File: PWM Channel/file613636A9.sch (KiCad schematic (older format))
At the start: 4 parts

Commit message: Starting rough routing
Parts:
- gave numbers to parts that had none: 4
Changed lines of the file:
@@
 U 1 1 61365705
 P 4050 3650
-F 0 "#PWR?" H 4050 3400 50  0001 C CNN
+AR Path="/61351170/61365705" Ref="#PWR?"  Part="1"
+AR Path="/613636AA/61365705" Ref="#PWR0103"  Part="1"
+F 0 "#PWR0103" H 4050 3400 50  0001 C CNN
 F 1 "GND" V 4055 3522 50  0000 R CNN
 F 2 "" H 4050 3650 50  0001 C CNN
@@
 U 1 1 6136570C
 P 3550 2750
-F 0 "#PWR?" H 3550 2600 50  0001 C CNN
+AR Path="/61351170/6136570C" Ref="#PWR?"  Part="1"
+AR Path="/613636AA/6136570C" Ref="#PWR0104"  Part="1"
+F 0 "#PWR0104" H 3550 2600 50  0001 C CNN
 F 1 "+5V" V 3565 2878 50  0000 L CNN
 F 2 "" H 3550 2750 50  0001 C CNN
@@
 AR Path="/613546BD/61365713" Ref="C?"  Part="1"
 AR Path="/61351170/61365713" Ref="C?"  Part="1"
-F 0 "C?" H 3635 1904 50  0000 R CNN
+AR Path="/613636AA/61365713" Ref="C401"  Part="1"
+F 0 "C401" H 3635 1904 50  0000 R CNN
 F 1 "0.1uF" H 3635 1995 50  0000 R CNN
 F 2 "Capacitor_THT:C_Disc_D4.3mm_W1.9mm_P5.00mm" H 3788 1800 50  0001 C CNN
@@
 U 1 1 61365719
 P 4050 1700
-F 0 "#PWR?" H 4050 1550 50  0001 C CNN
+AR Path="/61351170/61365719" Ref="#PWR?"  Part="1"
+AR Path="/613636AA/61365719" Ref="#PWR0105"  Part="1"
+F 0 "#PWR0105" H 4050 1550 50  0001 C CNN
 F 1 "+5V" H 4065 1873 50  0000 C CNN
 F 2 "" H 4050 1700 50  0001 C CNN
@@
 U 1 1 61365724
 P 3200 3050
-F 0 "#PWR?" H 3200 2800 50  0001 C CNN
+AR Path="/61351170/61365724" Ref="#PWR?"  Part="1"
+AR Path="/613636AA/61365724" Ref="#PWR0106"  Part="1"
+F 0 "#PWR0106" H 3200 2800 50  0001 C CNN
 F 1 "GND" V 3205 2922 50  0000 R CNN
 F 2 "" H 3200 3050 50  0001 C CNN
@@
 U 1 1 6136572B
 P 4050 2850
-F 0 "U?" H 4050 3631 50  0000 C CNN
+AR Path="/61351170/6136572B" Ref="U?"  Part="1"
+AR Path="/613636AA/6136572B" Ref="U401"  Part="1"
+F 0 "U401" H 4050 3631 50  0000 C CNN
 F 1 "74HCT595" H 4050 3540 50  0000 C CNN
 F 2 "Package_DIP:DIP-16_W7.62mm_Socket" H 4050 2850 50  0001 C CNN
@@
 U 1 1 61365731
 P 3500 2100
-F 0 "#PWR?" H 3500 1850 50  0001 C CNN
+AR Path="/61351170/61365731" Ref="#PWR?"  Part="1"
+AR Path="/613636AA/61365731" Ref="#PWR0107"  Part="1"
+F 0 "#PWR0107" H 3500 1850 50  0001 C CNN
 F 1 "GND" V 3505 1972 50  0000 R CNN
 F 2 "" H 3500 2100 50  0001 C CNN
@@
 U 1 1 6136573C
 P 4050 6150
-F 0 "#PWR?" H 4050 5900 50  0001 C CNN
+AR Path="/61351170/6136573C" Ref="#PWR?"  Part="1"
+AR Path="/613636AA/6136573C" Ref="#PWR0108"  Part="1"
+F 0 "#PWR0108" H 4050 5900 50  0001 C CNN
 F 1 "GND" V 4055 6022 50  0000 R CNN
 F 2 "" H 4050 6150 50  0001 C CNN
@@
 U 1 1 61365743
 P 3550 5250
-F 0 "#PWR?" H 3550 5100 50  0001 C CNN
+AR Path="/61351170/61365743" Ref="#PWR?"  Part="1"
+AR Path="/613636AA/61365743" Ref="#PWR0109"  Part="1"
+F 0 "#PWR0109" H 3550 5100 50  0001 C CNN
 F 1 "+5V" V 3565 5378 50  0000 L CNN
 F 2 "" H 3550 5250 50  0001 C CNN
@@
 AR Path="/613546BD/6136574A" Ref="C?"  Part="1"
 AR Path="/61351170/6136574A" Ref="C?"  Part="1"
-F 0 "C?" H 3635 4404 50  0000 R CNN
+AR Path="/613636AA/6136574A" Ref="C402"  Part="1"
+F 0 "C402" H 3635 4404 50  0000 R CNN
 F 1 "0.1uF" H 3635 4495 50  0000 R CNN
 F 2 "Capacitor_THT:C_Disc_D4.3mm_W1.9mm_P5.00mm" H 3788 4300 50  0001 C CNN
@@
 U 1 1 61365750
 P 4050 4200
-F 0 "#PWR?" H 4050 4050 50  0001 C CNN
+AR Path="/61351170/61365750" Ref="#PWR?"  Part="1"
+AR Path="/613636AA/61365750" Ref="#PWR0110"  Part="1"
+F 0 "#PWR0110" H 4050 4050 50  0001 C CNN
 F 1 "+5V" H 4065 4373 50  0000 C CNN
 F 2 "" H 4050 4200 50  0001 C CNN
@@
 U 1 1 6136575B
 P 3200 5550
-F 0 "#PWR?" H 3200 5300 50  0001 C CNN
+AR Path="/61351170/6136575B" Ref="#PWR?"  Part="1"
+AR Path="/613636AA/6136575B" Ref="#PWR0111"  Part="1"
+F 0 "#PWR0111" H 3200 5300 50  0001 C CNN
 F 1 "GND" V 3205 5422 50  0000 R CNN
 F 2 "" H 3200 5550 50  0001 C CNN
@@
 U 1 1 61365762
 P 4050 5350
-F 0 "U?" H 4050 6131 50  0000 C CNN
+AR Path="/61351170/61365762" Ref="U?"  Part="1"
+AR Path="/613636AA/61365762" Ref="U402"  Part="1"
+F 0 "U402" H 4050 6131 50  0000 C CNN
 F 1 "74HCT595" H 4050 6040 50  0000 C CNN
 F 2 "Package_DIP:DIP-16_W7.62mm_Socket" H 4050 5350 50  0001 C CNN
@@
 U 1 1 61365769
 P 3500 4600
-F 0 "#PWR?" H 3500 4350 50  0001 C CNN
+AR Path="/61351170/61365769" Ref="#PWR?"  Part="1"
+AR Path="/613636AA/61365769" Ref="#PWR0112"  Part="1"
+F 0 "#PWR0112" H 3500 4350 50  0001 C CNN
 F 1 "GND" V 3505 4472 50  0000 R CNN
 F 2 "" H 3500 4600 50  0001 C CNN

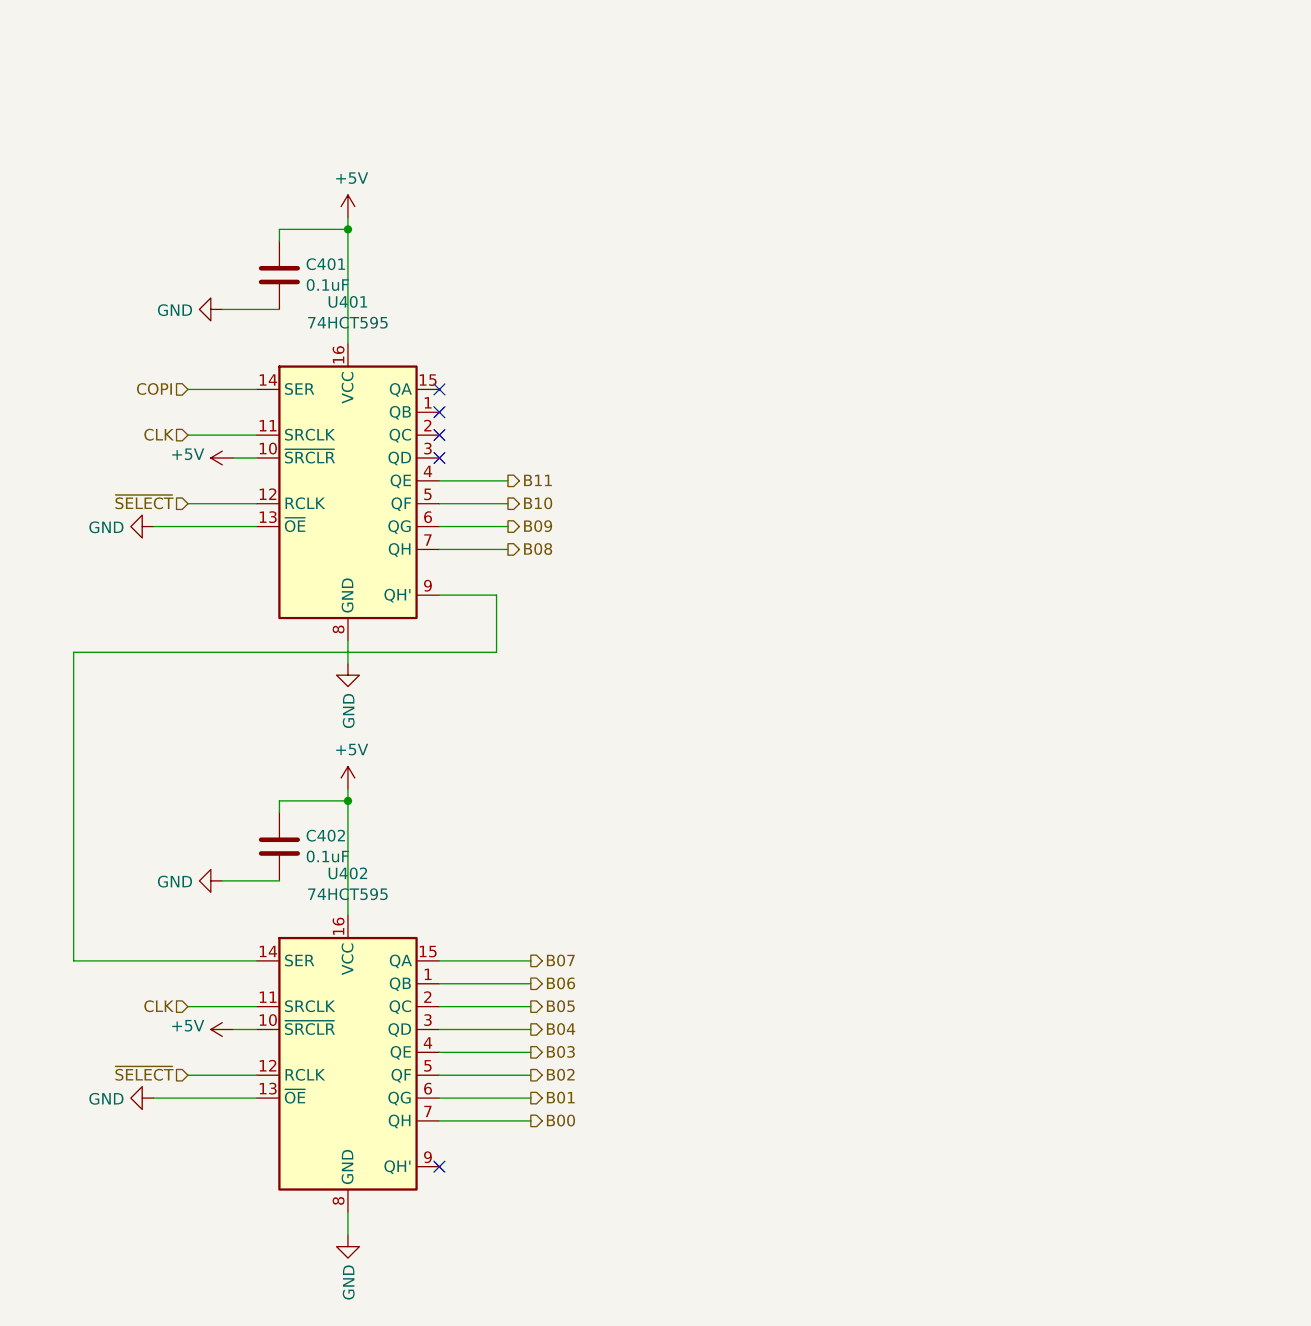
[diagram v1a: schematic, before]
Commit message: Updates to PWM Channel Board (#6)
Add a number of LED indicators and reduce from 12-bit to 8-bit
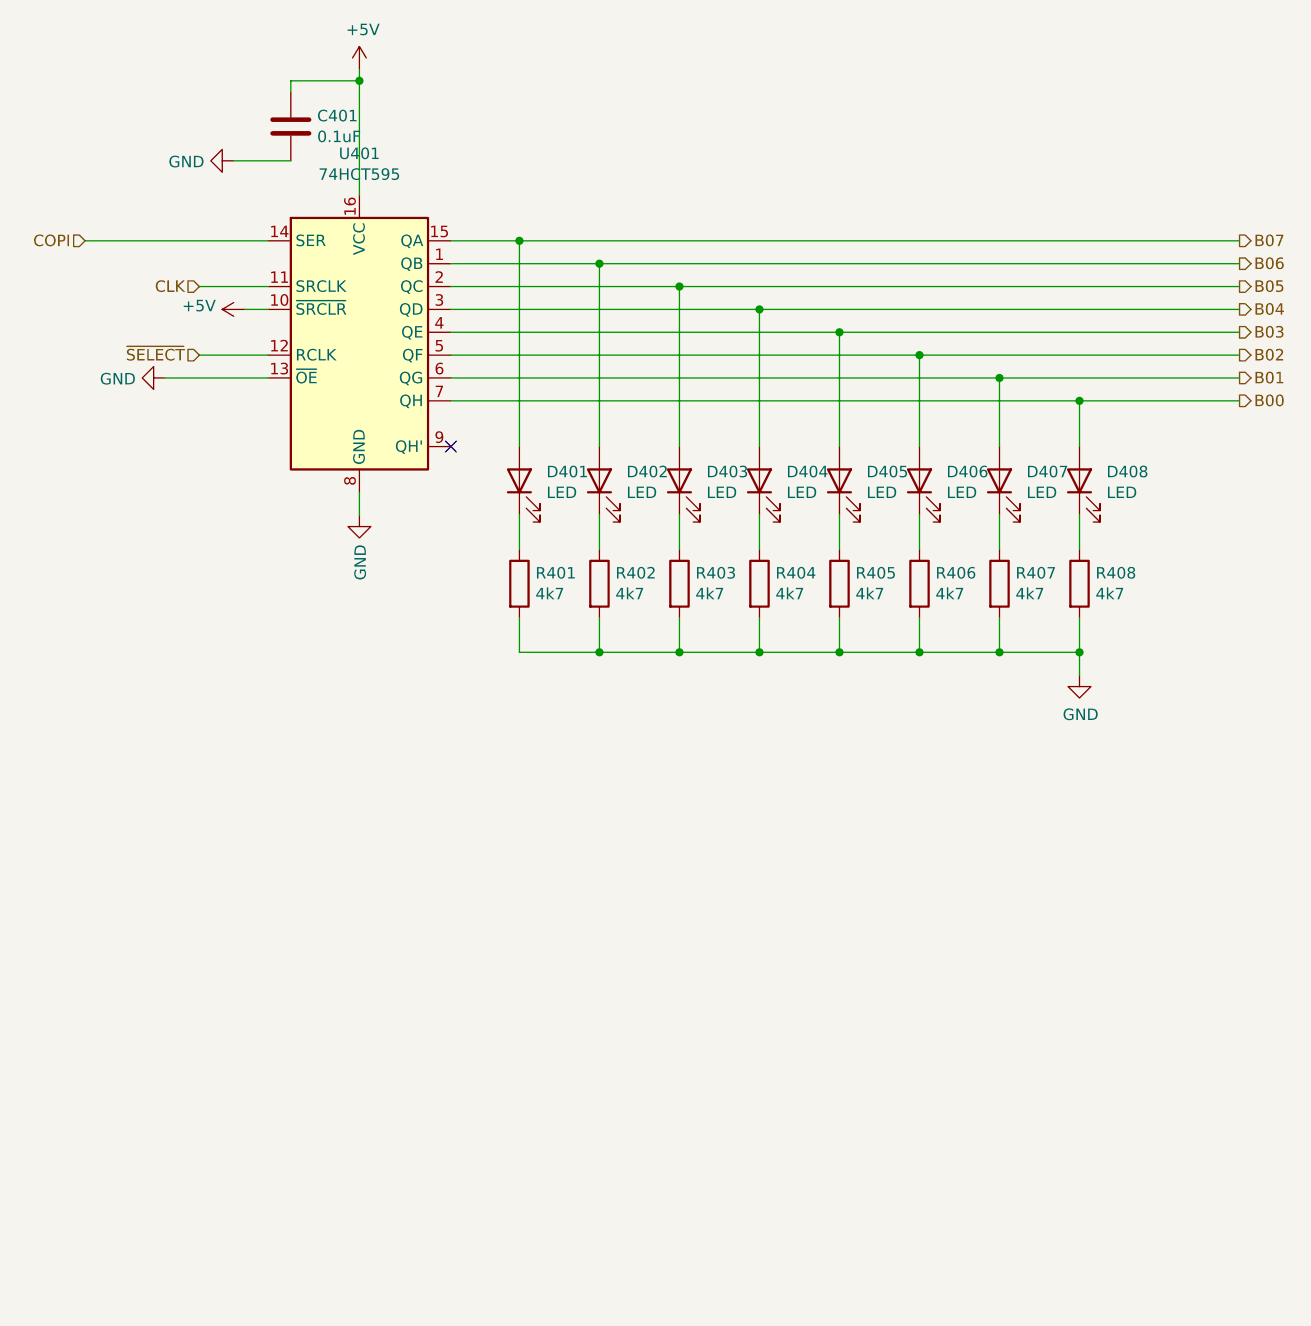
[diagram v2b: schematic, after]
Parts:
- removed C401: 0.1uF, Capacitor_THT:C_Disc_D4.3mm_W1.9mm_P5.00mm, symbol Device:C
- removed U401: 74HCT595, Package_DIP:DIP-16_W7.62mm_Socket, symbol 74xx:74HCT595
- added D401, D402, D403, D404, D405, D406, D407, D408: LED, LED_THT:LED_D3.0mm, symbol Device:LED
- added R401, R402, R403, R404, R405, R406, R407, R408: 4k7, Resistor_THT:R_Axial_DIN0207_L6.3mm_D2.5mm_P7.62mm_Horizontal, symbol Device:R
- renumbered C402 to C401, U402 to U401
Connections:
- net B00: now also D408.2 (A)
- net B01: now also D407.2 (A)
- net B02: now also D406.2 (A)
- net B03: now also D405.2 (A)
- net B04: now also D404.2 (A)
- net B05: now also D403.2 (A)
- net B06: now also D402.2 (A)
- net B07: now also D401.2 (A)
- net COPI: now also U401.14 (SER)
- net GND: now also R401.2, R402.2, R403.2, R404.2, R405.2, R406.2, R407.2, R408.2
- new net: D401.1 (K), R401.1
- new net: D402.1 (K), R402.1
- new net: D403.1 (K), R403.1
- new net: D404.1 (K), R404.1
- new net: D405.1 (K), R405.1
- new net: D406.1 (K), R406.1
- new net: D407.1 (K), R407.1
- new net: D408.1 (K), R408.1
- no-connect marks 5 -> 1
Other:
- moved on the sheet: C401, U401
